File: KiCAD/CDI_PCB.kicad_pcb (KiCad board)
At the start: 2 copper layers, 86.9 x 77.7 mm, 45 parts, among them P1 Blue, P10 Green w/ White, P11 Pink, P2 Black w/ White, P3 Yellow, P4 Green Coil, P5 Green Harness, P6 White, P7 Orange, P8 Brown, P9 Light Blue

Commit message: Shrink it down another 0.5in
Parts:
- moved R12 26.0 mm to (111.8, 71.1)
- moved D12 24.4 mm to (115.8, 74.2)
- moved P8 24.4 mm to (115.8, 68.6)
- moved P9 22.9 mm to (111.8, 66.0)
- moved P4 13.7 mm to (126.0, 103.6)
- moved P5 13.3 mm to (119.9, 103.6)
- moved D14 11.9 mm to (126.0, 95.0)
- moved P2 11.2 mm to (182.4, 104.1)
- moved P1 10.6 mm to (173.7, 103.6)
- moved D5 10.4 mm to (183.9, 99.1)
- moved R15 9.65 mm to (122.9, 78.7)
- moved P7 9.49 mm to (153.9, 103.6)
- moved P3 9.49 mm to (141.2, 103.6)
- moved P6 9.20 mm to (146.3, 103.6)
- moved D8 8.87 mm to (159.5, 104.6)
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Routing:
- net Net-(D10-Pad2): track 33.9 -> 22.5 mm
- net Net-(D12-Pad1): track 33.8 -> 23.8 mm
- net Net-(C1-Pad1): track 41.1 -> 49.6 mm
- net Net-(D6-Pad2): track 22.3 -> 15.5 mm
- net Net-(C2-Pad2): track 73.3 -> 68.1 mm
- net Net-(P10-Pad1): track 7.74 -> 4.27 mm
- net Net-(P9-Pad1): track 8.34 -> 5.08 mm
- net Net-(D2-Pad1): track 32.5 -> 29.3 mm
- net Net-(D9-Pad1): track 8.41 -> 5.33 mm
- net Net-(D11-Pad2): track 6.65 -> 9.70 mm
- net Net-(C1-Pad2): track 216.0 -> 218.4 mm
- net Net-(D5-Pad2): track 11.3 -> 9.06 mm
- net Net-(D11-Pad1): track 6.52 -> 4.99 mm
- net Net-(D5-Pad1): track 7.11 -> 5.66 mm
- net Net-(R4-Pad2): track 38.3 -> 37.0 mm
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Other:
- board size 86.9 x 77.7 mm -> 77.7 x 63 mm

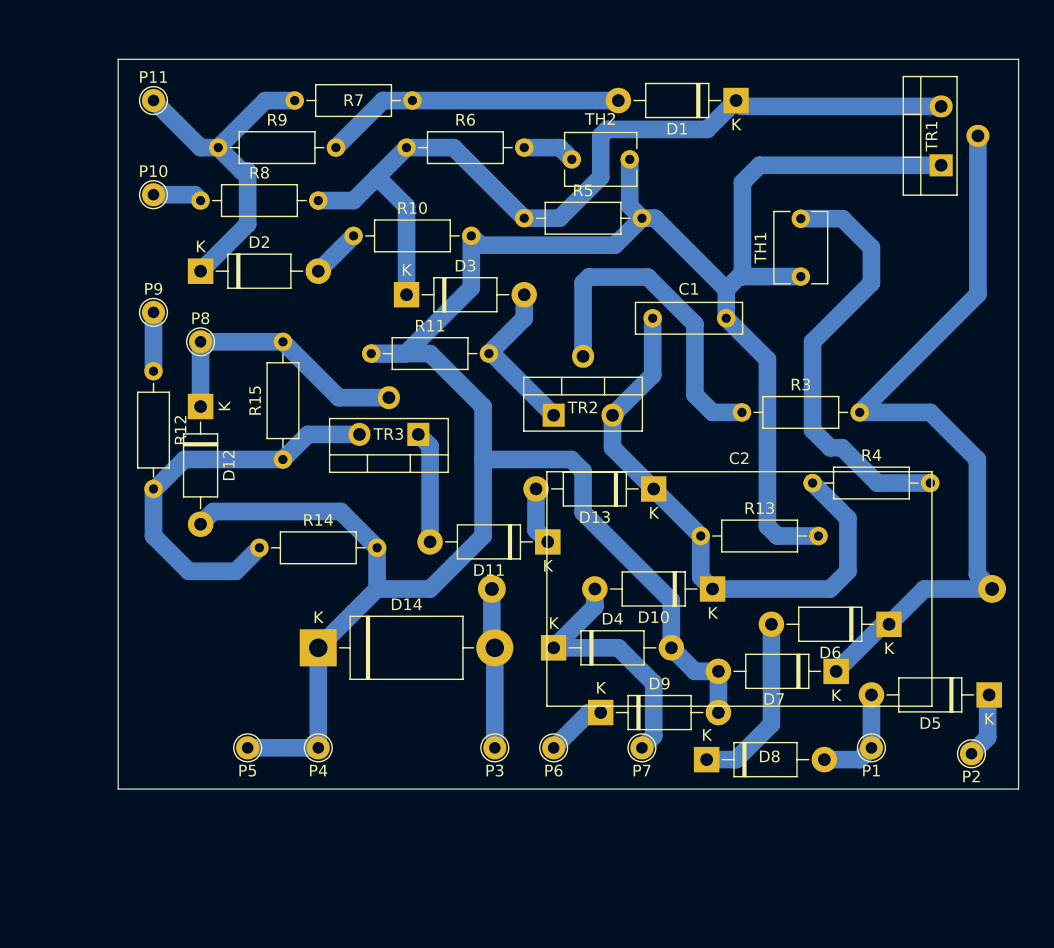
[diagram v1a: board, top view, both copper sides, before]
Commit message: Shrink the board size down to the original dimensions (69.8mm x 41.4mm) Add Rev3 gerber files as a zip. Add Rev4 gerber files (current version) as a zip. Add notes on making the harness.
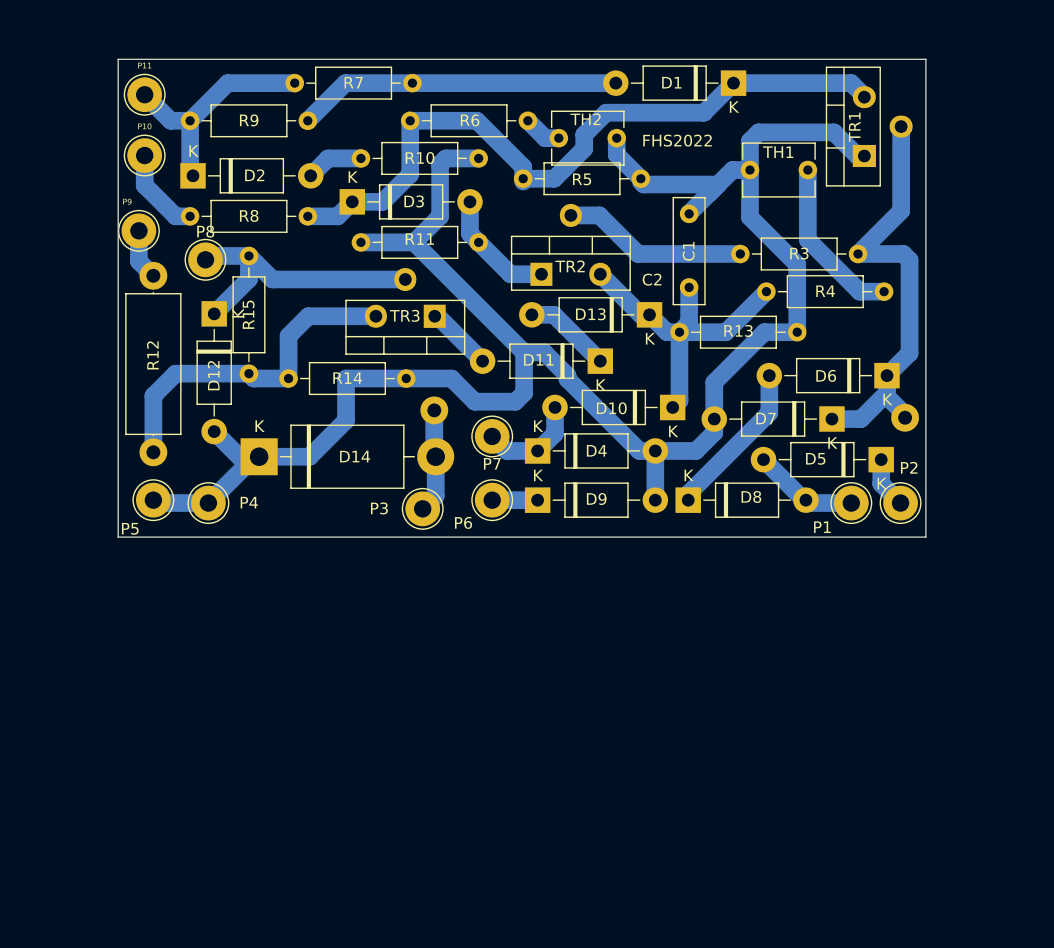
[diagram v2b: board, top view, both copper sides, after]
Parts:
- P1, P10, P11, P2, P3, P4, P5, P6, P7, P8, P9: footprint TestPoint:TestPoint_THTPad_D2.0mm_Drill1.0mm -> TestPoint:TestPoint_THTPad_D3.0mm_Drill1.5mm
- R12: footprint Resistor_THT:R_Axial_DIN0207_L6.3mm_D2.5mm_P10.16mm_Horizontal -> Resistor_THT:R_Axial_DIN0414_L11.9mm_D4.5mm_P15.24mm_Horizontal
- moved P7 29.8 mm to (141.0, 76.8)
- moved P4 23.2 mm to (116.5, 82.5)
- moved P5 22.9 mm to (111.8, 82.2)
- moved P2 22.5 mm to (176.2, 82.5)
- moved D8 22.5 mm to (157.9, 82.2)
- moved D5 22.3 mm to (174.6, 78.8)
- moved P6 22.0 mm to (141.0, 82.2)
- moved D7 21.8 mm to (170.3, 75.2)
- moved P3 21.6 mm to (135.0, 83.0)
- moved D6 21.5 mm to (175.1, 71.5)
- moved P1 21.2 mm to (172.0, 82.5)
- moved D9 19.1 mm to (144.9, 82.2)
- moved R13 17.7 mm to (157.2, 67.8)
- moved D14 17.3 mm to (120.9, 78.5)
- moved C2 17.1 mm to (141.1, 74.5)
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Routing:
- net Net-(C1-Pad2): track 218.4 -> 163.9 mm
- net Net-(C2-Pad2): track 68.1 -> 39.6 mm
- net Net-(R4-Pad2): track 37.0 -> 14.5 mm
- net Net-(C1-Pad1): track 49.6 -> 28.8 mm
- net Net-(D1-Pad1): track 75.9 -> 61.8 mm
- net Net-(D10-Pad2): track 22.5 -> 8.81 mm
- net Net-(R3-Pad1): track 28.7 -> 16.0 mm
- net Net-(D2-Pad1): track 29.3 -> 20.1 mm
- net Net-(R12-Pad2): track 34.9 -> 29.4 mm
- net Net-(C2-Pad1): track 13.8 -> 9.01 mm
- net Net-(D11-Pad2): track 9.70 -> 5.74 mm
- net Net-(D3-Pad2): track 14.1 -> 10.4 mm
- net Net-(P10-Pad1): track 4.27 -> 7.60 mm
- net Net-(D11-Pad1): track 4.99 -> 7.57 mm
- net Net-(D1-Pad2): track 26.1 -> 27.9 mm
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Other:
- board size 77.7 x 63 mm -> 69.7 x 41.2 mm
- board text added: "06-03-2022"
- board text added: "4"
- board text added: "FHS2022"
- board text removed: "05-24-2022"
- board text removed: "3"

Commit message: Revision 5:
Remove 'K' on F Silkscreen layer.
Add mounting two mounting holes in case someone wants it.
Move TH1 down a bit so TR1 can bend back for room.
Move Pin 2 of TR2 closer to 1 and 3 to make it a bit easier to add to the board
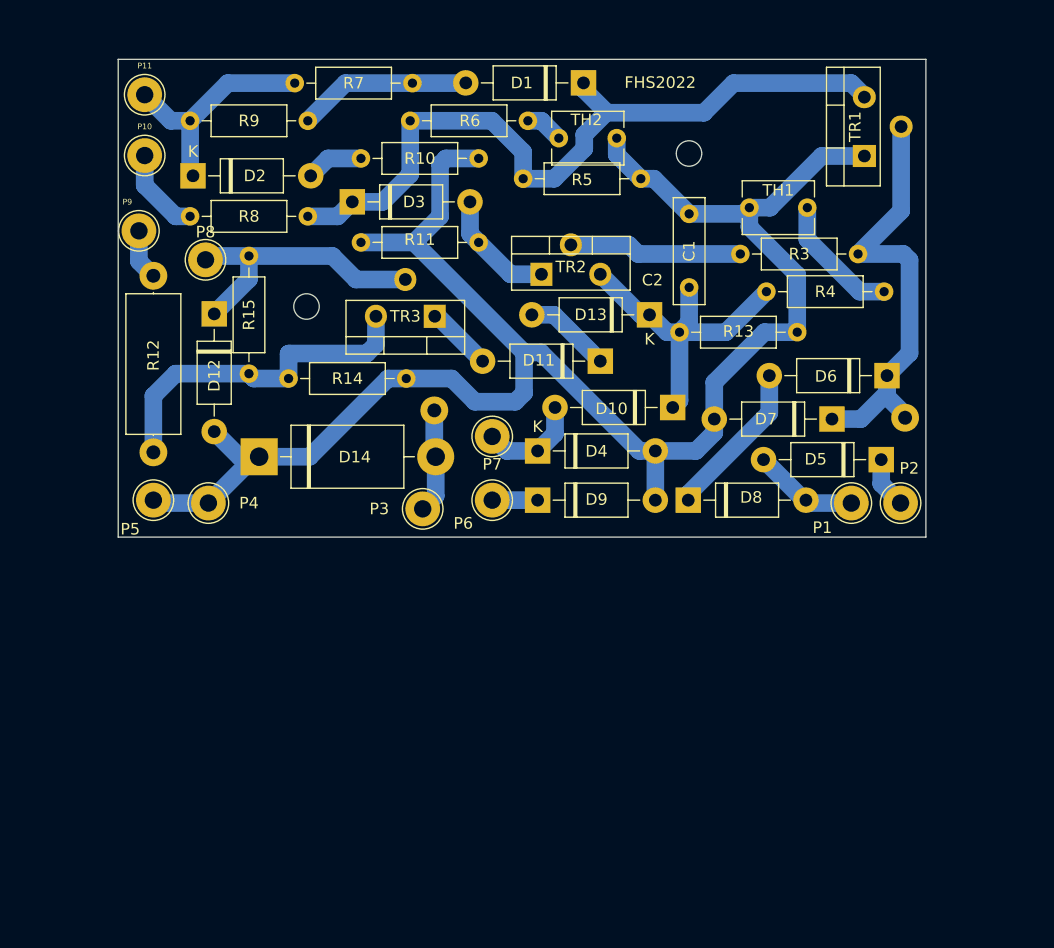
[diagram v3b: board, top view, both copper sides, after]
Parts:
- added H1: MountingHole, MountingHole:MountingHole_2.2mm_M2, F.Cu at (125.0, 65.5)
- added H2: MountingHole, MountingHole:MountingHole_2.2mm_M2, F.Cu at (158.0, 52.3)
- moved D1 13.0 mm to (148.9, 46.2)
- moved TH1 3.25 mm to (163.2, 57.0)
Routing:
- net Net-(D1-Pad2): track 27.9 -> 15.0 mm
- net Net-(C1-Pad2): track 163.9 -> 152.1 mm
- net Net-(D1-Pad1): track 61.8 -> 65.6 mm
- net Net-(R4-Pad2): track 14.5 -> 11.2 mm
- net Net-(R3-Pad1): track 16.0 -> 15.0 mm
- net Net-(R12-Pad2): track 29.4 -> 29.9 mm
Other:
- board text added: "06-10-2022"
- board text added: "5"
- board text removed: "06-03-2022"
- board text removed: "4"
